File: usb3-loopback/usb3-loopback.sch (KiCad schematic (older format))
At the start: 1 part

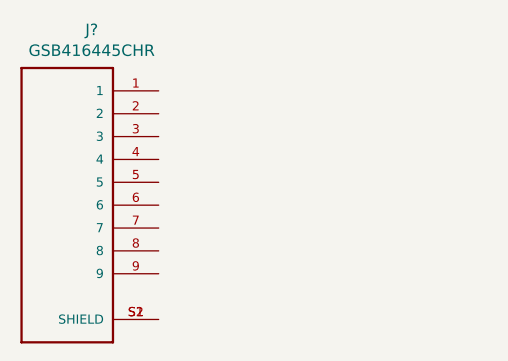
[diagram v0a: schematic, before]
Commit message: usb-loopback: as submitted
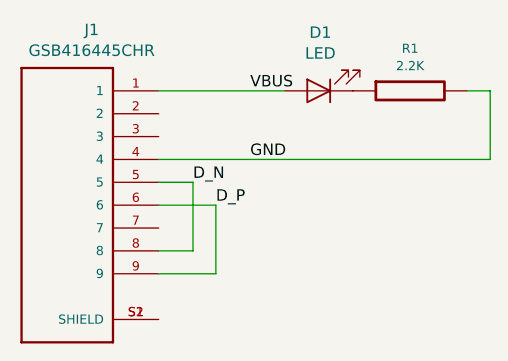
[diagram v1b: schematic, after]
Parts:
- added D1: LED, tom-passives:C_0805_2012Metric, symbol tom-opto:LED
- added R1: 2.2K, tom-passives:R_0603_1608Metric, symbol tom-passives:R
- gave numbers to parts that had none: 1
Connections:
- net VBUS: now reaches J1.1
- net VBUS: now also D1.2 (A)
- net GND: now reaches J1.4
- net GND: now also R1.2
- net D_N: now reaches J1.5
- net D_N: now also J1.8
- net D_P: now reaches J1.6
- net D_P: now also J1.9
- new net: D1.1 (K), R1.1
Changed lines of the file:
@@
 $EndDescr
 $Comp
-L usb3-loopback:GSB416445CHR J?
+L usb3-loopback:GSB416445CHR J1
 U 1 1 5F2C35A3
 P 4350 3050
-F 0 "J?" H 4243 3817 50  0000 C CNN
+F 0 "J1" H 4243 3817 50  0000 C CNN
 F 1 "GSB416445CHR" H 4243 3726 50  0000 C CNN
 F 2 "usb3-loopback:AMPHENOL_GSB416445CHR" H 4350 3050 50  0001 L BNN
@@
 EndData
 $EndBitmap
+Wire Wire Line
+	4750 2950 4900 2950
+Wire Wire Line
+	4900 2950 4900 3250
+Wire Wire Line
+	4900 3250 4750 3250
+Wire Wire Line
+	4750 3050 5000 3050
+Wire Wire Line
+	5000 3050 5000 3350
+Wire Wire Line
+	5000 3350 4750 3350
+Text Label 4900 2950 0    50   ~ 0
+D_N
+Text Label 5000 3050 0    50   ~ 0
+D_P
+$Comp
+L tom-opto:LED D1
+U 1 1 5F2C4750
+P 5450 2550
+F 0 "D1" H 5443 2295 50  0000 C CNN
+F 1 "LED" H 5443 2386 50  0000 C CNN
+F 2 "tom-passives:C_0805_2012Metric" H 5450 2550 50  0001 C CNN
+F 3 "~" H 5450 2550 50  0001 C CNN
+	1    5450 2550
+	-1   0    0    1
+$EndComp
+Wire Wire Line
+	4750 2550 5300 2550
+$Comp
+L tom-passives:R R1
+U 1 1 5F2C5EE1
+P 5850 2550
+F 0 "R1" V 5665 2550 40  0000 C CNN
+F 1 "2.2K" V 5741 2550 40  0000 C CNN
+F 2 "tom-passives:R_0603_1608Metric" V 5780 2550 30  0001 C CNN
+F 3 "" H 5850 2550 30  0000 C CNN
+	1    5850 2550
+	0    -1   1    0
+$EndComp
+Wire Wire Line
+	6100 2550 6200 2550
+Wire Wire Line
+	6200 2850 4750 2850
+Wire Wire Line
+	6200 2550 6200 2850
+Text Label 5150 2850 0    50   ~ 0
+GND
+Text Label 5150 2550 0    50   ~ 0
+VBUS
 $EndSCHEMATC
